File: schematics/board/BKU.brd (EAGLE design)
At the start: 94 x 94 mm, 60 parts

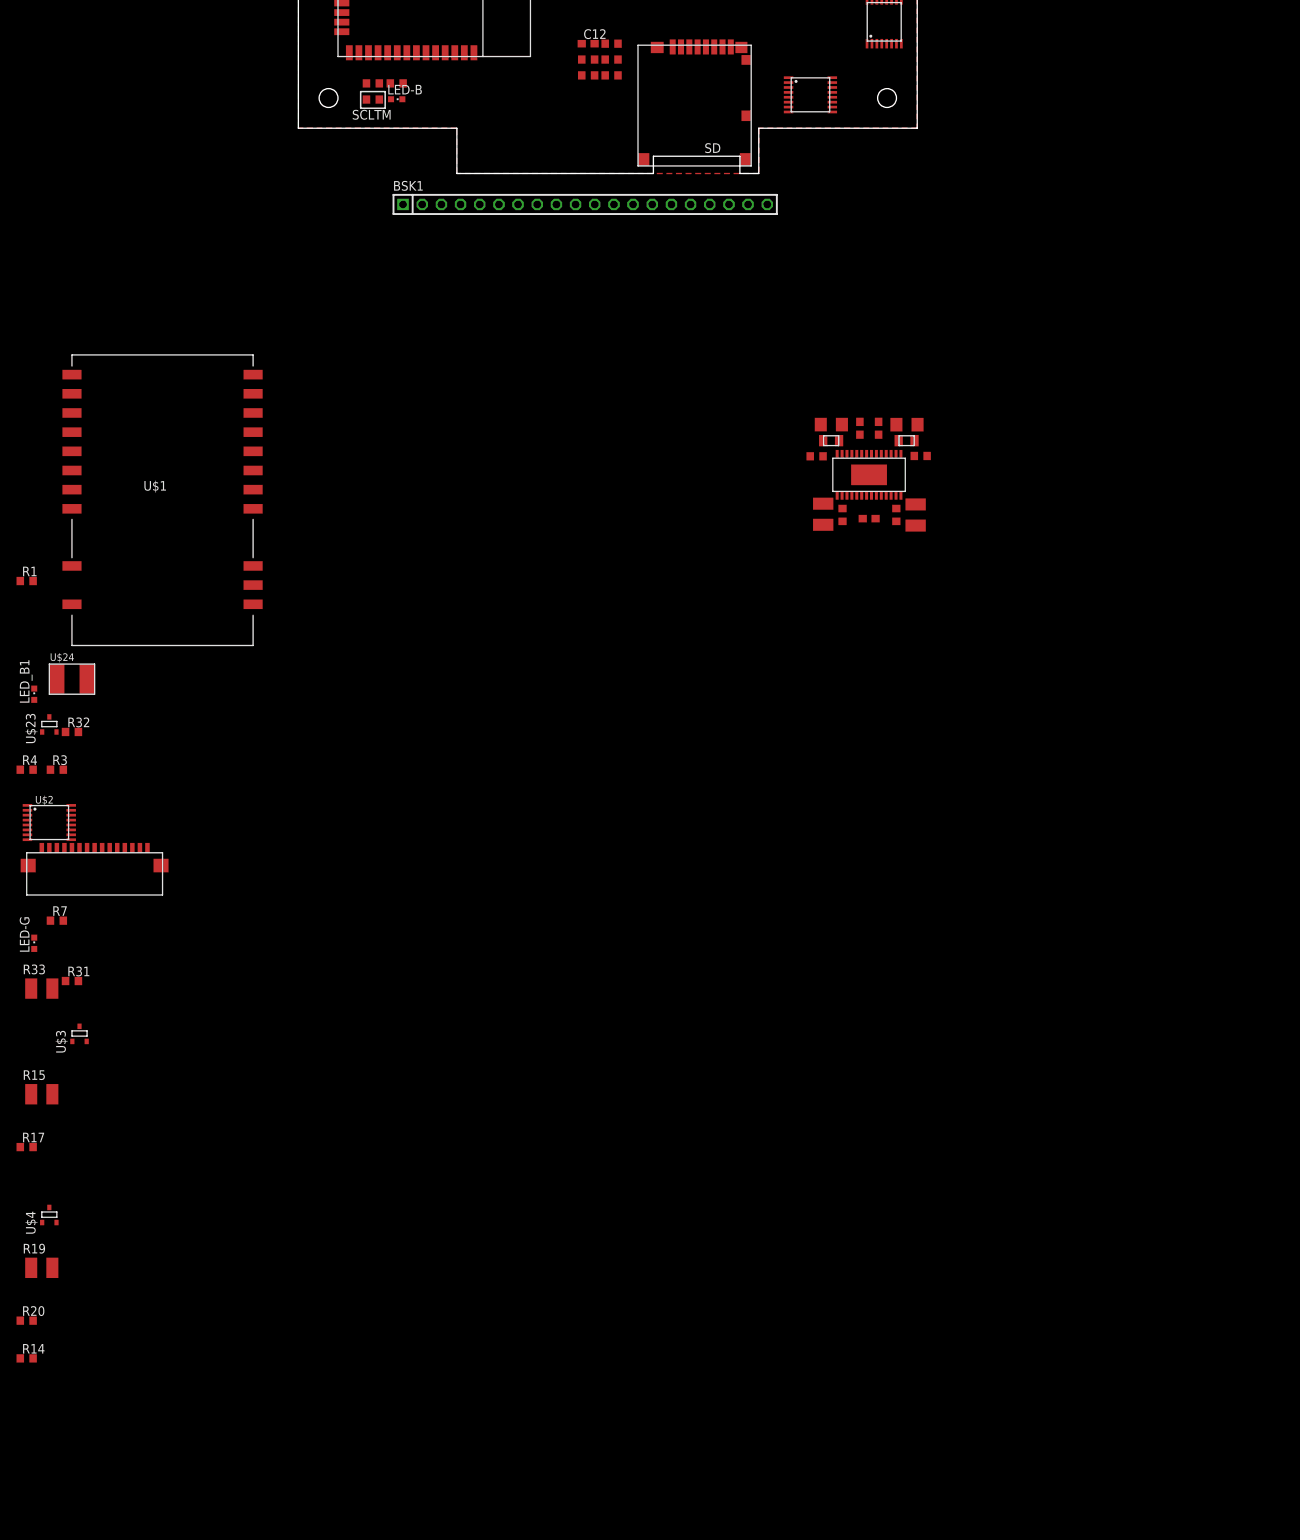
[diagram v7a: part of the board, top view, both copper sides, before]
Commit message: Сделана схема БКУ
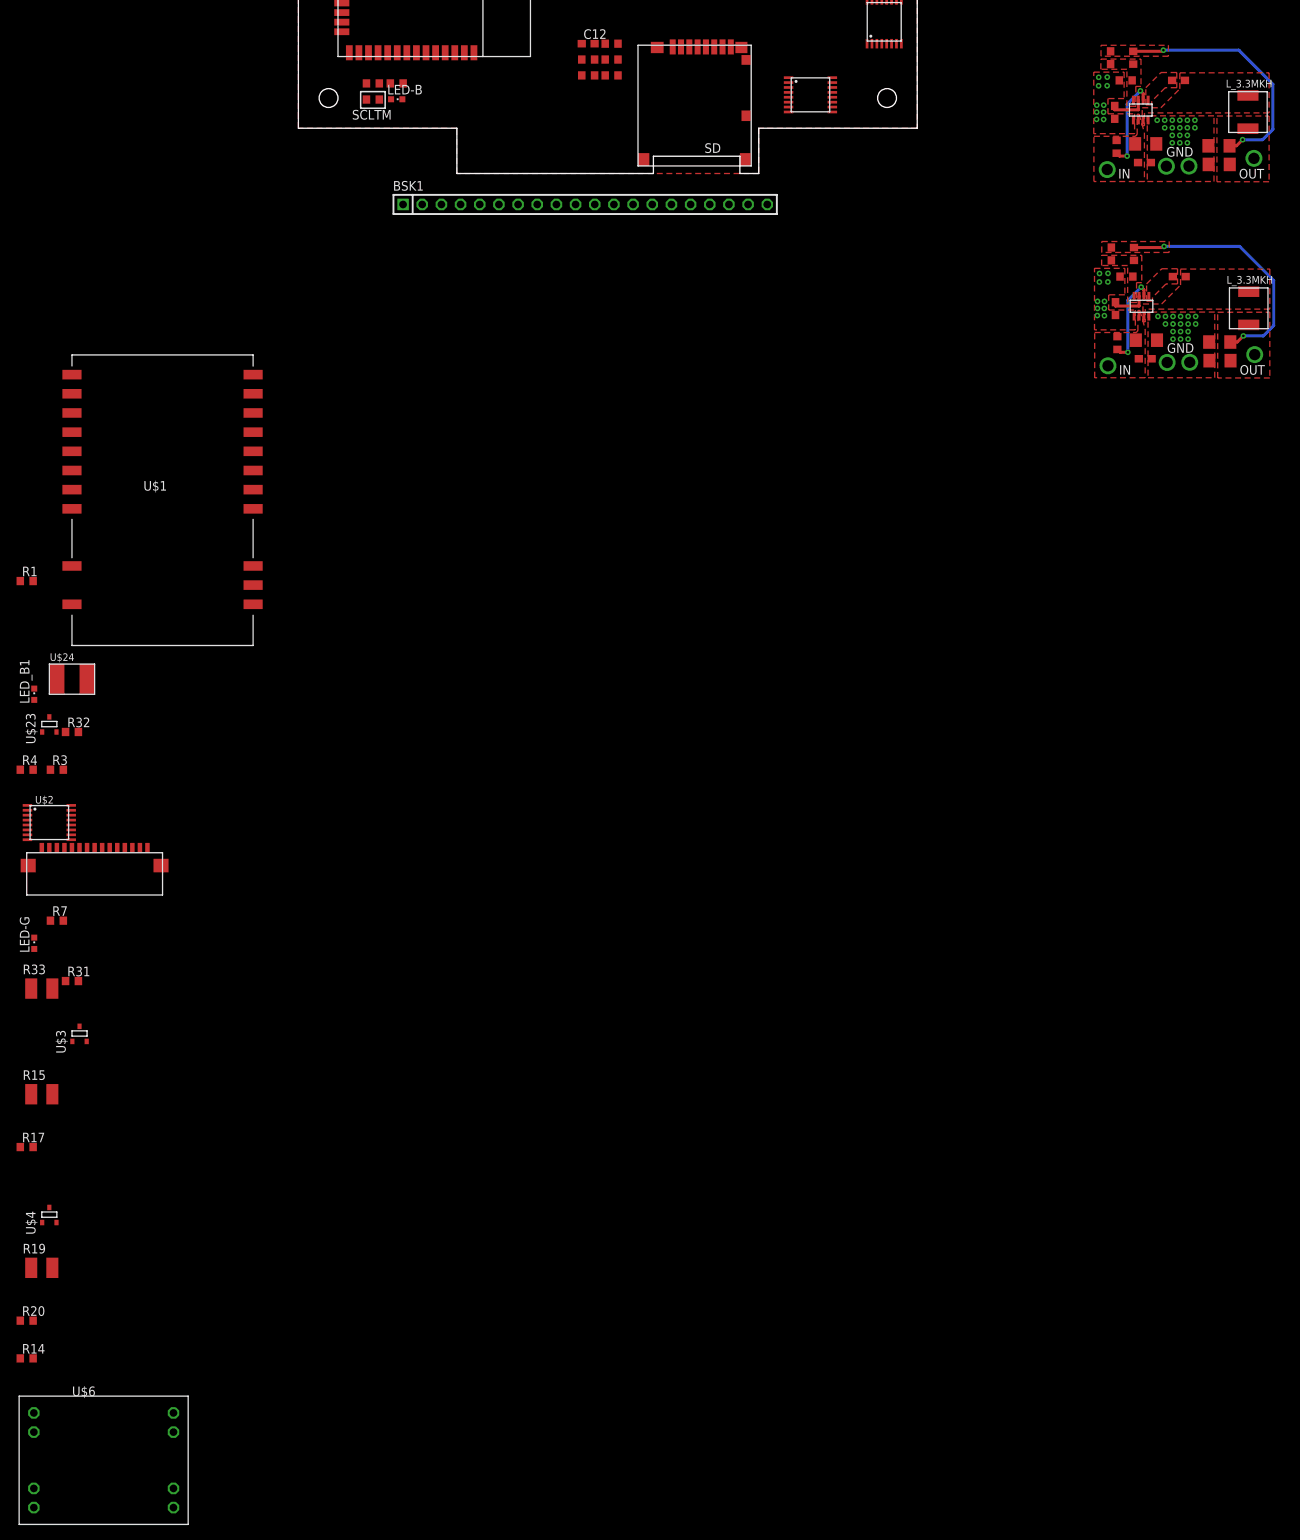
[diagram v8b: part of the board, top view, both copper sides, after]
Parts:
- removed R12: 73,2k, resistor:R0603
- removed R13: 45,3k, resistor:R0603
- removed R8, R9: 10k, resistor:R0603
- removed U$10: LTC3633, CanCubeSat:LTC3633
- removed U$11: 1µH, CanCubeSat:B82498F
- removed U$12: B82498F, CanCubeSat:B82498F
- added C10, C7, C8: 0,1µ, rcl:C0603
- added C11: 33p, rcl:C0603
- added C13, C2, C9: 22µ, rcl:C1206
- added L_3.3, L_3.3-1: L_3.3MKH, CanCubeSat:L_SPM5020
- added MP2225, MP2225-1: MP2225, CanCubeSat:TSOT23-8
- added R16, R27: 100k, resistor:R0603
- added R25, R28: 40k2, resistor:R0603
- added R26, R29: 8k87, resistor:R0603
- added U$6: MP1584-B, CanCubeSat:MP1584-B
- C1, C5: value 0,1µ -> 22µ; device rcl:C0603 -> rcl:C1206
- C14: value 2,2µ -> 0,1µ
- C15: value 22µ -> 0,1µ; device rcl:C1206 -> rcl:C0603
- C16: value 47µ -> 33p; device rcl:C1210 -> rcl:C0603
- C17: value 47µ -> 0,1µ; device rcl:C1210 -> rcl:C0603
- moved C5 49.0 mm to (128.1, -22.3), turned to 0 degrees
- moved C17 47.4 mm to (114.3, -17.9), turned to 90 degrees
- moved C1 46.1 mm to (128.1, -24.8), turned to 0 degrees
- moved C16 43.2 mm to (113.7, -10.7)
- moved C6 43.2 mm to (118.4, -22.1), turned to 180 degrees
- moved C14 42.3 mm to (118.2, -24.6)
- moved C15 41.1 mm to (122.7, -13.7)
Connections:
- removed net N$24: C14.2, U$10.1, U$10.14, U$10.21, U$10.22, U$10.5, U$10.7, U$10.8
- removed net N$25: R13.1, R8.1, U$10.3
- removed net N$28: C5.1, U$10.26, U$11.1
- removed net N$31: C5.2, U$10.23
- removed net N$32: C1.1, U$10.20
- removed net N$33: C1.2, U$10.16, U$12.1
- removed net N$39: R12.1, R9.1, U$10.12
- new net N$10: MP2225-1.P$6, R27.2
- new net N$12: C17.2, MP2225-1.P$7
- new net N$13: C7.2, MP2225.P$5
- new net N$14: C7.1, L_3.3.P$2, MP2225.P$3
- new net N$15: MP2225.P$6, R16.2
- new net N$16: C8.2, MP2225.P$7
- new net N$20: C11.2, MP2225.P$8, R25.1, R26.1
- new net N$21: C10.2, C9.2, MP2225.P$2, R16.1
- new net N$22: C16.2, MP2225-1.P$8, R28.1, R29.1
- new net N$7: C14.2, C6.2, MP2225-1.P$2, R27.1
- new net N$8: C15.1, L_3.3-1.P$2, MP2225-1.P$3
- new net N$9: C15.2, MP2225-1.P$5
- net 3V3: now also C11.1, C13.2, C2.2, L_3.3.P$1, R25.2, U$6.P$7, U$6.P$8; no longer C6.1, R13.2, U$10.28, U$11.2
- net 5V: now also C1.2, C16.1, C5.2, L_3.3-1.P$1, R28.2; no longer C15.1, R12.2, U$10.15, U$12.2
- net BUS+: now also U$6.P$1, U$6.P$2; no longer C16.1, C17.1, U$10.18, U$10.24, U$10.6, U$10.9
- net GND: no longer C14.1, C15.2, C16.2, C17.2, C6.2, R8.2, R9.2, U$10.10, U$10.HEAT
- net GND-OUT: now also C1.1, C10.1, C13.1, C14.1, C17.1, C2.1, C5.1, C6.1, C8.1, C9.1, MP2225-1.P$1, MP2225-1.P$4, MP2225.P$1, MP2225.P$4, R26.2, R29.2, U$6.P$3, U$6.P$4, U$6.P$5, U$6.P$6
- net RX-EN: now also U$1.7; no longer U$1.6
- net TX-EN: now also U$1.6; no longer U$1.7
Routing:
- net 5V: track 0.00 -> 33.1 mm, vias 0 -> 3
- net 3V3: track 0.00 -> 33.1 mm, vias 0 -> 3
- net N$10: track 0.00 -> 12.3 mm, vias 0 -> 2
- net N$15: track 0.00 -> 12.3 mm, vias 0 -> 2
- net N$12: track 0.00 -> 5.00 mm
- net N$16: track 0.00 -> 5.00 mm
- added copper zone on layer 1, net 3V3
- added copper zone on layer 1, net 5V
- added copper zone on layer 1, net GND-OUT
- added copper zone on layer 1, net N$13
- added copper zone on layer 1, net N$14
- added copper zone on layer 1, net N$20
- added copper zone on layer 1, net N$21
- added copper zone on layer 1, net N$22
- added copper zone on layer 1, net N$7
- added copper zone on layer 1, net N$8
- added copper zone on layer 1, net N$9
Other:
- board text added: "GND"
- board text added: "IN"
- board text added: "MP2225"
- board text added: "OUT"
